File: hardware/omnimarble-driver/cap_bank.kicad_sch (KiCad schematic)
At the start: 12 parts, among them J2 AUX-BANK, U3 MCP6002

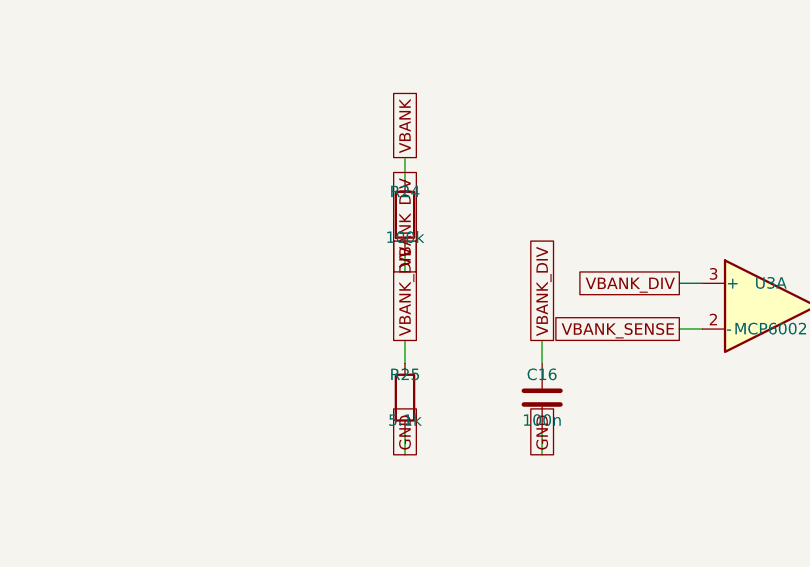
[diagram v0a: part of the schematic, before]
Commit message: Address external design review: boost FB + OVP redesign, BOM freeze
Review findings accepted and fixed (each verified by machine check):

1. Boost feedback network was wrong (confirmed: as-drawn spanned
   54-68V with PWM inverted vs the comment). Redesigned: RT/RB/RJ =
   100k/10k/9.1k with the exact transfer function documented in the
   schematic and design-calcs.md. PWM=0 (MCU-dead state) commands
   55.0V; full PWM commands 18.7V (below the 24.5V converter floor).
   New calcs.py asserts both endpoints.
2. OVP tripped at 55.6V, not the claimed 63V (confirmed). Redesigned:
   CJ431 (+/-0.5%) + 100k/4.3k 1% -> 60.5V nominal, 59.1-62.0V across
   tolerances. Protection ladder asserted in calcs.py: 55V operating
   < 59.1V trip-min, 62.0V trip-max < 63V cap rating - 1V. Operating
   ceiling deliberately reduced 60->55V to keep the bands disjoint.
3. BOM/schematic controller split-brain: bom.csv was stale
   (pre-UC3843 swap); regenerated from parts.py. Both now UC3843B.
4. High-power placeholders now real orderable parts (LCSC-verified):
   47R/5W SQM cement C5807995, dump redesigned to 2x 100R/10W cement
   in series C216413 (no 20-25W part stocked on LCSC; 5.3s to <5V),
   50mR/3W 2512 C2994645, 63V/35V electrolytics C28241/C176666, 10uH
   Sunlord C79272, MINI fuses+Keystone 3568 holders, buzzer, Pico
   sockets/breakout headers. Single documented exception: the 6.8k/2W
   bleed (CRH2512J6K80E04Z) is marked ORDER-REVIEW because LCSC's
   search is uncrawlable - validate.py allowlists it visibly.
5. validate.py pulled forward from the fab phase: fails on unknown
   footprints, blank LCSC on machine-placed parts, missing Variant
   fields, and duplicate refs; generates per-variant gate-rail BOMs
   (bom_rail_emit/recv.csv). Caught two bad footprint names.
6. Paralleling constraints now on the schematic (same-lot FETs,
   symmetric copper, <25mm gate loops, driver return at shunt star).
7. Fail-safe defaults hardened: MCU_FIRE and FIRE_GATED get explicit
   pulldow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
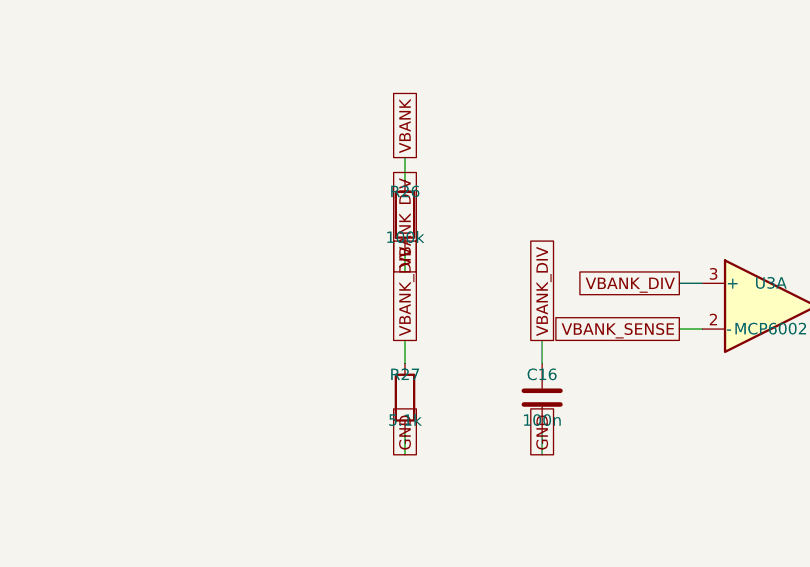
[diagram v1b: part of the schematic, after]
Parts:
- removed R24: 100k, Resistor_SMD:R_0603_1608Metric, symbol Device:R
- removed R25: 5.1k, Resistor_SMD:R_0603_1608Metric, symbol Device:R
- added R26: 100k, Resistor_SMD:R_0603_1608Metric, symbol Device:R
- added R27: 5.1k, Resistor_SMD:R_0603_1608Metric, symbol Device:R
- F2: LCSC C207030 -> C5249699
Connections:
- net GND: now also R27.2
- net VBANK: now also R26.1
- net VBANK_DIV: now also R26.2, R27.1
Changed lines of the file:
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@@
 		(instances
 			(project "omnimarble-driver"
-				(path "/73d8eff6-39f1-4e5f-a80b-a36699d4dd7c/3fdb0994-c492-4402-ba13-446e089d2362"
+				(path "/324ed851-0be4-493c-900d-5ec8847c0520/52d4c111-46bf-4480-a236-9942de1bb3ff"
 					(reference "C90")
 					(unit 1)
@@
 		(instances
 			(project "omnimarble-driver"
-				(path "/73d8eff6-39f1-4e5f-a80b-a36699d4dd7c/3fdb0994-c492-4402-ba13-446e089d2362"
+				(path "/324ed851-0be4-493c-900d-5ec8847c0520/52d4c111-46bf-4480-a236-9942de1bb3ff"
 					(reference "C91")
 					(unit 1)
@@
 		(instances
 			(project "omnimarble-driver"
-				(path "/73d8eff6-39f1-4e5f-a80b-a36699d4dd7c/3fdb0994-c492-4402-ba13-446e089d2362"
+				(path "/324ed851-0be4-493c-900d-5ec8847c0520/52d4c111-46bf-4480-a236-9942de1bb3ff"
 					(reference "C92")
 					(unit 1)
@@
 		(instances
 			(project "omnimarble-driver"
-				(path "/73d8eff6-39f1-4e5f-a80b-a36699d4dd7c/3fdb0994-c492-4402-ba13-446e089d2362"
+				(path "/324ed851-0be4-493c-900d-5ec8847c0520/52d4c111-46bf-4480-a236-9942de1bb3ff"
 					(reference "C93")
 					(unit 1)
@@
 		(instances
 			(project "omnimarble-driver"
-				(path "/73d8eff6-39f1-4e5f-a80b-a36699d4dd7c/3fdb0994-c492-4402-ba13-446e089d2362"
+				(path "/324ed851-0be4-493c-900d-5ec8847c0520/52d4c111-46bf-4480-a236-9942de1bb3ff"
 					(reference "C94")
 					(unit 1)
@@
 		(instances
 			(project "omnimarble-driver"
-				(path "/73d8eff6-39f1-4e5f-a80b-a36699d4dd7c/3fdb0994-c492-4402-ba13-446e089d2362"
+				(path "/324ed851-0be4-493c-900d-5ec8847c0520/52d4c111-46bf-4480-a236-9942de1bb3ff"
 					(reference "J2")
 					(unit 1)
@@
 			)
 		)
-		(property "LCSC" "C207030"
+		(property "LCSC" "C5249699"
 			(at 180.34 90.17 0)
 			(show_name no)
@@
 		(instances
 			(project "omnimarble-driver"
-				(path "/73d8eff6-39f1-4e5f-a80b-a36699d4dd7c/3fdb0994-c492-4402-ba13-446e089d2362"
+				(path "/324ed851-0be4-493c-900d-5ec8847c0520/52d4c111-46bf-4480-a236-9942de1bb3ff"
 					(reference "F2")
 					(unit 1)
@@
 		(on_board yes)
 		(dnp no)
-		(property "Reference" "R24"
+		(property "Reference" "R26"
 			(at 59.69 116.84 0)
 			(show_name no)
@@
 		(instances
 			(project "omnimarble-driver"
-				(path "/73d8eff6-39f1-4e5f-a80b-a36699d4dd7c/3fdb0994-c492-4402-ba13-446e089d2362"
-					(reference "R24")
+				(path "/324ed851-0be4-493c-900d-5ec8847c0520/52d4c111-46bf-4480-a236-9942de1bb3ff"
+					(reference "R26")
 					(unit 1)
 				)
@@
 		(on_board yes)
 		(dnp no)
-		(property "Reference" "R25"
+		(property "Reference" "R27"
 			(at 59.69 137.16 0)
 			(show_name no)
@@
 		(instances
 			(project "omnimarble-driver"
-				(path "/73d8eff6-39f1-4e5f-a80b-a36699d4dd7c/3fdb0994-c492-4402-ba13-446e089d2362"
-					(reference "R25")
+				(path "/324ed851-0be4-493c-900d-5ec8847c0520/52d4c111-46bf-4480-a236-9942de1bb3ff"
+					(reference "R27")
 					(unit 1)
 				)
@@
 		(instances
 			(project "omnimarble-driver"
-				(path "/73d8eff6-39f1-4e5f-a80b-a36699d4dd7c/3fdb0994-c492-4402-ba13-446e089d2362"
+				(path "/324ed851-0be4-493c-900d-5ec8847c0520/52d4c111-46bf-4480-a236-9942de1bb3ff"
 					(reference "C16")
 					(unit 1)
@@
 		(instances
 			(project "omnimarble-driver"
-				(path "/73d8eff6-39f1-4e5f-a80b-a36699d4dd7c/3fdb0994-c492-4402-ba13-446e089d2362"
+				(path "/324ed851-0be4-493c-900d-5ec8847c0520/52d4c111-46bf-4480-a236-9942de1bb3ff"
 					(reference "U3")
 					(unit 1)
@@
 		(instances
 			(project "omnimarble-driver"
-				(path "/73d8eff6-39f1-4e5f-a80b-a36699d4dd7c/3fdb0994-c492-4402-ba13-446e089d2362"
+				(path "/324ed851-0be4-493c-900d-5ec8847c0520/52d4c111-46bf-4480-a236-9942de1bb3ff"
 					(reference "U3")
 					(unit 3)
@@
 		(instances
 			(project "omnimarble-driver"
-				(path "/73d8eff6-39f1-4e5f-a80b-a36699d4dd7c/3fdb0994-c492-4402-ba13-446e089d2362"
+				(path "/324ed851-0be4-493c-900d-5ec8847c0520/52d4c111-46bf-4480-a236-9942de1bb3ff"
 					(reference "C17")
 					(unit 1)
@@
 		(instances
 			(project "omnimarble-driver"
-				(path "/73d8eff6-39f1-4e5f-a80b-a36699d4dd7c/3fdb0994-c492-4402-ba13-446e089d2362"
+				(path "/324ed851-0be4-493c-900d-5ec8847c0520/52d4c111-46bf-4480-a236-9942de1bb3ff"
 					(reference "#PWR0011")
 					(unit 1)

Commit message: Datasheet-exact footprints, placement engine, scripted PCB router WIP
- gen_footprints.py: TOLL-8, D2PAK (cathode-tab corrected), 5930 shunt,
  9.5mm barrier, HF3FF relay land patterns; drop _DRAFT footprints
- placement.py: 220x150 board plan, pulse zone polygons derived from
  package pad windows, shelf-packed clusters, Kelvin/manual tracks
- gen_pcb.py: netlist->board generator with zone builder, via stitching,
  pad-in-zone assertions, straggler/GND-drop/escape pre-routes and a
  negotiated-congestion (PathFinder-lite) signal router + greedy cleanup
- debug_route.py/debug_map.py/debug_j7.py: router diagnostics

Co-Authored-By: Claude Fable 5 <noreply@anthropic.com>
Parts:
- J2: footprint omnimarble:TerminalBarrier_1x02_P9.50mm_DRAFT -> omnimarble:TerminalBarrier_1x02_P9.50mm
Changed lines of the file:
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@@
 		(instances
 			(project "omnimarble-driver"
-				(path "/70e4f6fa-a16c-43fd-8b02-c5feb48cd6d1/09f45a2a-6a6a-469b-877a-84170f6c473d"
+				(path "/be74192f-67ac-494b-9ef4-1b59d4ce9fe4/509670b2-7640-42fc-b2b2-dc39736afa50"
 					(reference "C90")
 					(unit 1)
@@
 		(instances
 			(project "omnimarble-driver"
-				(path "/70e4f6fa-a16c-43fd-8b02-c5feb48cd6d1/09f45a2a-6a6a-469b-877a-84170f6c473d"
+				(path "/be74192f-67ac-494b-9ef4-1b59d4ce9fe4/509670b2-7640-42fc-b2b2-dc39736afa50"
 					(reference "C91")
 					(unit 1)
@@
 		(instances
 			(project "omnimarble-driver"
-				(path "/70e4f6fa-a16c-43fd-8b02-c5feb48cd6d1/09f45a2a-6a6a-469b-877a-84170f6c473d"
+				(path "/be74192f-67ac-494b-9ef4-1b59d4ce9fe4/509670b2-7640-42fc-b2b2-dc39736afa50"
 					(reference "C92")
 					(unit 1)
@@
 		(instances
 			(project "omnimarble-driver"
-				(path "/70e4f6fa-a16c-43fd-8b02-c5feb48cd6d1/09f45a2a-6a6a-469b-877a-84170f6c473d"
+				(path "/be74192f-67ac-494b-9ef4-1b59d4ce9fe4/509670b2-7640-42fc-b2b2-dc39736afa50"
 					(reference "C93")
 					(unit 1)
@@
 		(instances
 			(project "omnimarble-driver"
-				(path "/70e4f6fa-a16c-43fd-8b02-c5feb48cd6d1/09f45a2a-6a6a-469b-877a-84170f6c473d"
+				(path "/be74192f-67ac-494b-9ef4-1b59d4ce9fe4/509670b2-7640-42fc-b2b2-dc39736afa50"
 					(reference "C94")
 					(unit 1)
@@
 			)
 		)
-		(property "Footprint" "omnimarble:TerminalBarrier_1x02_P9.50mm_DRAFT"
+		(property "Footprint" "omnimarble:TerminalBarrier_1x02_P9.50mm"
 			(at 180.34 59.69 0)
 			(show_name no)
@@
 		(instances
 			(project "omnimarble-driver"
-				(path "/70e4f6fa-a16c-43fd-8b02-c5feb48cd6d1/09f45a2a-6a6a-469b-877a-84170f6c473d"
+				(path "/be74192f-67ac-494b-9ef4-1b59d4ce9fe4/509670b2-7640-42fc-b2b2-dc39736afa50"
 					(reference "J2")
 					(unit 1)
@@
 		(instances
 			(project "omnimarble-driver"
-				(path "/70e4f6fa-a16c-43fd-8b02-c5feb48cd6d1/09f45a2a-6a6a-469b-877a-84170f6c473d"
+				(path "/be74192f-67ac-494b-9ef4-1b59d4ce9fe4/509670b2-7640-42fc-b2b2-dc39736afa50"
 					(reference "F2")
 					(unit 1)
@@
 		(instances
 			(project "omnimarble-driver"
-				(path "/70e4f6fa-a16c-43fd-8b02-c5feb48cd6d1/09f45a2a-6a6a-469b-877a-84170f6c473d"
+				(path "/be74192f-67ac-494b-9ef4-1b59d4ce9fe4/509670b2-7640-42fc-b2b2-dc39736afa50"
 					(reference "R26")
 					(unit 1)
@@
 		(instances
 			(project "omnimarble-driver"
-				(path "/70e4f6fa-a16c-43fd-8b02-c5feb48cd6d1/09f45a2a-6a6a-469b-877a-84170f6c473d"
+				(path "/be74192f-67ac-494b-9ef4-1b59d4ce9fe4/509670b2-7640-42fc-b2b2-dc39736afa50"
 					(reference "R27")
 					(unit 1)
@@
 		(instances
 			(project "omnimarble-driver"
-				(path "/70e4f6fa-a16c-43fd-8b02-c5feb48cd6d1/09f45a2a-6a6a-469b-877a-84170f6c473d"
+				(path "/be74192f-67ac-494b-9ef4-1b59d4ce9fe4/509670b2-7640-42fc-b2b2-dc39736afa50"
 					(reference "C16")
 					(unit 1)
@@
 		(instances
 			(project "omnimarble-driver"
-				(path "/70e4f6fa-a16c-43fd-8b02-c5feb48cd6d1/09f45a2a-6a6a-469b-877a-84170f6c473d"
+				(path "/be74192f-67ac-494b-9ef4-1b59d4ce9fe4/509670b2-7640-42fc-b2b2-dc39736afa50"
 					(reference "U3")
 					(unit 1)
@@
 		(instances
 			(project "omnimarble-driver"
-				(path "/70e4f6fa-a16c-43fd-8b02-c5feb48cd6d1/09f45a2a-6a6a-469b-877a-84170f6c473d"
+				(path "/be74192f-67ac-494b-9ef4-1b59d4ce9fe4/509670b2-7640-42fc-b2b2-dc39736afa50"
 					(reference "U3")
 					(unit 3)
@@
 		(instances
 			(project "omnimarble-driver"
-				(path "/70e4f6fa-a16c-43fd-8b02-c5feb48cd6d1/09f45a2a-6a6a-469b-877a-84170f6c473d"
+				(path "/be74192f-67ac-494b-9ef4-1b59d4ce9fe4/509670b2-7640-42fc-b2b2-dc39736afa50"
 					(reference "C17")
 					(unit 1)
@@
 		(instances
 			(project "omnimarble-driver"
-				(path "/70e4f6fa-a16c-43fd-8b02-c5feb48cd6d1/09f45a2a-6a6a-469b-877a-84170f6c473d"
+				(path "/be74192f-67ac-494b-9ef4-1b59d4ce9fe4/509670b2-7640-42fc-b2b2-dc39736afa50"
 					(reference "#PWR0011")
 					(unit 1)

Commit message: Snapshot driver's final validated state before parking as vNext
Fold the last regeneration into the repo so the source is internally consistent
with the already-committed board/BOM (the Q90 diode->MOSFET fix + JLC cart
substitutions previously landed only in the root schematic + board):
- 7 driver schematic sub-sheets, regenerated to carry the final part numbers.
- fab/jlc/ORDER_NOTES.md — final BOM (J2/J5 C707836, R21/R22 C5110275, etc.).
- omnimarble-driver-5-rev-39.ses — the routing session import-clean rebuilds the
  board from; committing it keeps the routed board reproducible while parked.

Timestamp-only gerber/zip churn and scratch (.ses iterations, drc/erc reports,
logs) were left out. Driver stays vNext/on-hold per V0_BENCH_RIG.md.

Co-Authored-By: Claude Opus 4.8 <noreply@anthropic.com>
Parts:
- J2: LCSC C60785 -> C707836
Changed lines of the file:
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@@
 		(instances
 			(project "omnimarble-driver"
-				(path "/4f6b9534-97fd-44ae-b81e-62754cb6cba6/75055750-43d3-41e0-a7c5-b3ca2e7420e9"
+				(path "/e983a447-c241-422e-9650-13442643de66/b6fe2580-d622-43fc-8716-bce18c62b63c"
 					(reference "C90")
 					(unit 1)
@@
 		(instances
 			(project "omnimarble-driver"
-				(path "/4f6b9534-97fd-44ae-b81e-62754cb6cba6/75055750-43d3-41e0-a7c5-b3ca2e7420e9"
+				(path "/e983a447-c241-422e-9650-13442643de66/b6fe2580-d622-43fc-8716-bce18c62b63c"
 					(reference "C91")
 					(unit 1)
@@
 		(instances
 			(project "omnimarble-driver"
-				(path "/4f6b9534-97fd-44ae-b81e-62754cb6cba6/75055750-43d3-41e0-a7c5-b3ca2e7420e9"
+				(path "/e983a447-c241-422e-9650-13442643de66/b6fe2580-d622-43fc-8716-bce18c62b63c"
 					(reference "C92")
 					(unit 1)
@@
 		(instances
 			(project "omnimarble-driver"
-				(path "/4f6b9534-97fd-44ae-b81e-62754cb6cba6/75055750-43d3-41e0-a7c5-b3ca2e7420e9"
+				(path "/e983a447-c241-422e-9650-13442643de66/b6fe2580-d622-43fc-8716-bce18c62b63c"
 					(reference "C93")
 					(unit 1)
@@
 		(instances
 			(project "omnimarble-driver"
-				(path "/4f6b9534-97fd-44ae-b81e-62754cb6cba6/75055750-43d3-41e0-a7c5-b3ca2e7420e9"
+				(path "/e983a447-c241-422e-9650-13442643de66/b6fe2580-d622-43fc-8716-bce18c62b63c"
 					(reference "C94")
 					(unit 1)
@@
 			)
 		)
-		(property "LCSC" "C60785"
+		(property "LCSC" "C707836"
 			(at 180.34 59.69 0)
 			(show_name no)
@@
 		(instances
 			(project "omnimarble-driver"
-				(path "/4f6b9534-97fd-44ae-b81e-62754cb6cba6/75055750-43d3-41e0-a7c5-b3ca2e7420e9"
+				(path "/e983a447-c241-422e-9650-13442643de66/b6fe2580-d622-43fc-8716-bce18c62b63c"
 					(reference "J2")
 					(unit 1)
@@
 		(instances
 			(project "omnimarble-driver"
-				(path "/4f6b9534-97fd-44ae-b81e-62754cb6cba6/75055750-43d3-41e0-a7c5-b3ca2e7420e9"
+				(path "/e983a447-c241-422e-9650-13442643de66/b6fe2580-d622-43fc-8716-bce18c62b63c"
 					(reference "F2")
 					(unit 1)
@@
 		(instances
 			(project "omnimarble-driver"
-				(path "/4f6b9534-97fd-44ae-b81e-62754cb6cba6/75055750-43d3-41e0-a7c5-b3ca2e7420e9"
+				(path "/e983a447-c241-422e-9650-13442643de66/b6fe2580-d622-43fc-8716-bce18c62b63c"
 					(reference "R26")
 					(unit 1)
@@
 		(instances
 			(project "omnimarble-driver"
-				(path "/4f6b9534-97fd-44ae-b81e-62754cb6cba6/75055750-43d3-41e0-a7c5-b3ca2e7420e9"
+				(path "/e983a447-c241-422e-9650-13442643de66/b6fe2580-d622-43fc-8716-bce18c62b63c"
 					(reference "R27")
 					(unit 1)
@@
 		(instances
 			(project "omnimarble-driver"
-				(path "/4f6b9534-97fd-44ae-b81e-62754cb6cba6/75055750-43d3-41e0-a7c5-b3ca2e7420e9"
+				(path "/e983a447-c241-422e-9650-13442643de66/b6fe2580-d622-43fc-8716-bce18c62b63c"
 					(reference "C16")
 					(unit 1)
@@
 		(instances
 			(project "omnimarble-driver"
-				(path "/4f6b9534-97fd-44ae-b81e-62754cb6cba6/75055750-43d3-41e0-a7c5-b3ca2e7420e9"
+				(path "/e983a447-c241-422e-9650-13442643de66/b6fe2580-d622-43fc-8716-bce18c62b63c"
 					(reference "U3")
 					(unit 1)
@@
 		(instances
 			(project "omnimarble-driver"
-				(path "/4f6b9534-97fd-44ae-b81e-62754cb6cba6/75055750-43d3-41e0-a7c5-b3ca2e7420e9"
+				(path "/e983a447-c241-422e-9650-13442643de66/b6fe2580-d622-43fc-8716-bce18c62b63c"
 					(reference "U3")
 					(unit 3)
@@
 		(instances
 			(project "omnimarble-driver"
-				(path "/4f6b9534-97fd-44ae-b81e-62754cb6cba6/75055750-43d3-41e0-a7c5-b3ca2e7420e9"
+				(path "/e983a447-c241-422e-9650-13442643de66/b6fe2580-d622-43fc-8716-bce18c62b63c"
 					(reference "C17")
 					(unit 1)
@@
 		(instances
 			(project "omnimarble-driver"
-				(path "/4f6b9534-97fd-44ae-b81e-62754cb6cba6/75055750-43d3-41e0-a7c5-b3ca2e7420e9"
+				(path "/e983a447-c241-422e-9650-13442643de66/b6fe2580-d622-43fc-8716-bce18c62b63c"
 					(reference "#PWR0011")
 					(unit 1)
